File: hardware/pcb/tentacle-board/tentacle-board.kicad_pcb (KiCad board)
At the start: 2 copper layers, 55 x 55 mm, 74 parts, among them IC1 W25Q32JVZPIQ, J3 Conn_01x02, J5 Motor, J6 Motor, U1 NCP1117-3.3_SOT223, U3 RP2040, U4 DRV8825PWP, U5 DRV8825PWP, Y1 ABM8-12.000MHZ-20-B1U-T

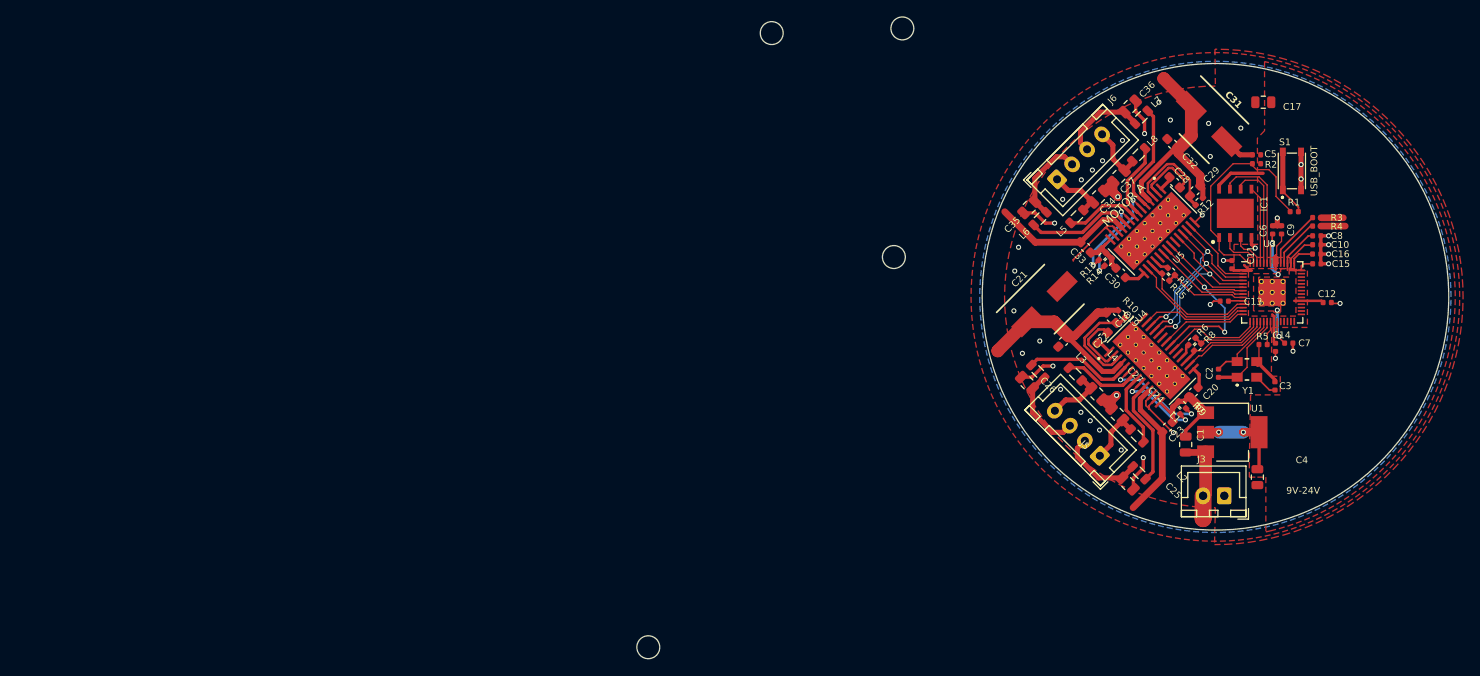
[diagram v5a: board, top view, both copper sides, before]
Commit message: Added aux plugs and updated the edge cuts
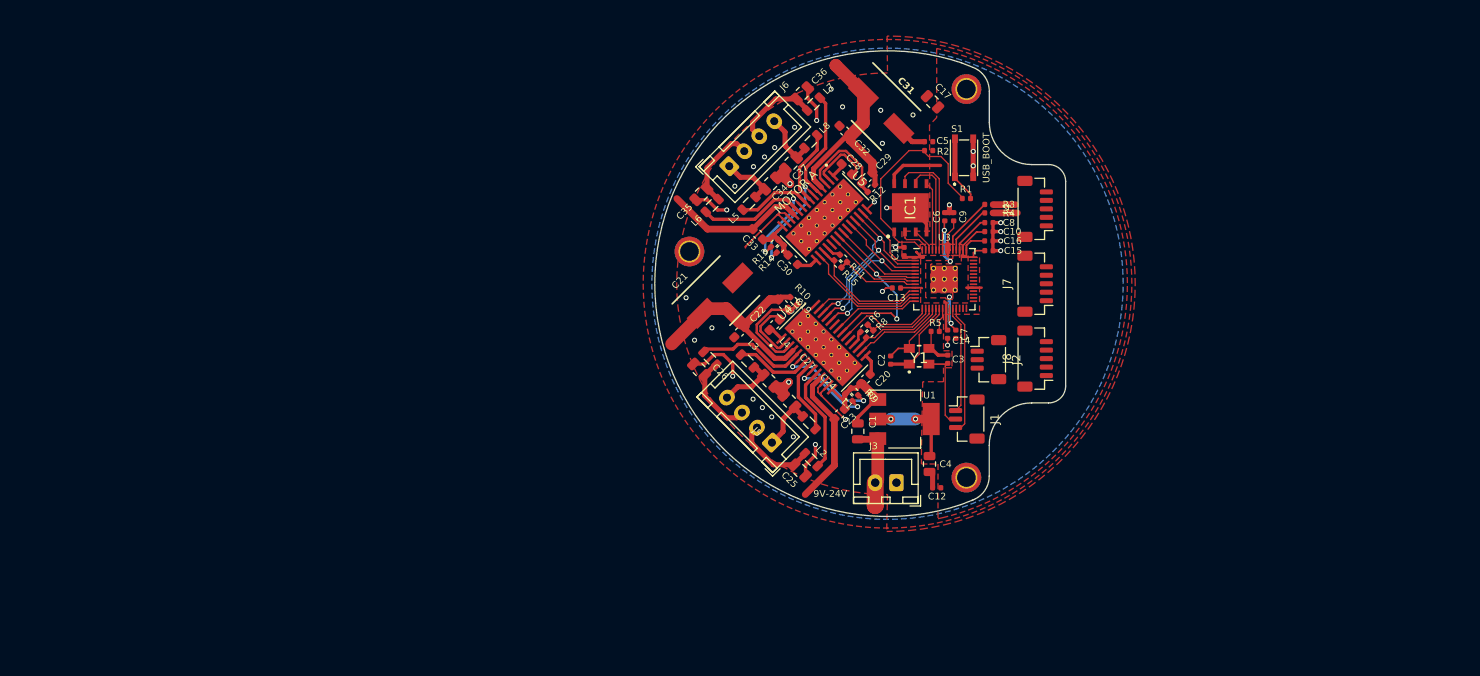
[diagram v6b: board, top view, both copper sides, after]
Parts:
- removed H2: MountingHole, MountingHole:MountingHole_2.7mm_M2.5
- added J1: DEBUG, Connector_JST:JST_SH_BM03B-SRSS-TB_1x03-1MP_P1.00mm_Vertical, F.Cu at (128.1, 109.7)
- added J2: UART0, Connector_JST:JST_SH_BM03B-SRSS-TB_1x03-1MP_P1.00mm_Vertical, F.Cu at (130.6, 102.7)
- added J4: Conn_01x05, Connector_JST:JST_SH_BM05B-SRSS-TB_1x05-1MP_P1.00mm_Vertical, F.Cu at (136.1, 84.9)
- added J7: Conn_01x05, Connector_JST:JST_SH_BM05B-SRSS-TB_1x05-1MP_P1.00mm_Vertical, F.Cu at (136.1, 93.7)
- added J8: Conn_01x05, Connector_JST:JST_SH_BM05B-SRSS-TB_1x05-1MP_P1.00mm_Vertical, F.Cu at (136.1, 102.5)
- H1, H3, H4: footprint MountingHole:MountingHole_2.7mm_M2.5 -> MountingHole:MountingHole_2.2mm_M2_ISO7380_Pad_TopBottom
- moved H4 75.7 mm to (128.0, 70.8)
- moved C12 51.0 mm to (124.5, 117.8), turned to 180 degrees
- moved C7 39.3 mm to (126.8, 99.7), turned to -90 degrees
- moved C17 39.0 mm to (124.0, 72.2), turned to 135 degrees
- moved C3 38.7 mm to (125.8, 102.6)
- moved L1 38.7 mm to (109.5, 110.1)
- moved R14 38.7 mm to (106.1, 89.6)
- moved C10 38.7 mm to (130.7, 87.5)
- moved C11 38.7 mm to (120.7, 89.9)
- moved C14 38.7 mm to (125.8, 99.6)
- moved C15 38.7 mm to (130.7, 89.8)
- moved C18 38.7 mm to (105.4, 98.5)
- moved C19 38.7 mm to (106.5, 96.2)
- moved C26 38.7 mm to (96.5, 103.8)
- moved C27 38.7 mm to (104.8, 105.1)
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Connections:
- IC1 pad 9: unconnected-(IC1-EP-Pad9) -> GND
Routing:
- net /SWD: track 0.00 -> 15.3 mm
- net GND: track 86.5 -> 101.2 mm, vias 40 -> 35
- net /SWCLK: track 0.00 -> 12.7 mm
- net +3V3: track 54.4 -> 52.4 mm
- net /QSPI_SD2: track 4.17 -> 2.78 mm
- net /QSPI_SD3: track 15.0 -> 13.8 mm
- net /QSPI_SCLK: track 12.9 -> 11.6 mm
- net /QSPI_SD1: track 5.17 -> 3.99 mm
- net Net-(Y1-X2): track 5.47 -> 4.42 mm
- net /QSPI_SD0: track 9.16 -> 8.11 mm
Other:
- board size 55 x 55 mm -> 48.4 x 54.9 mm

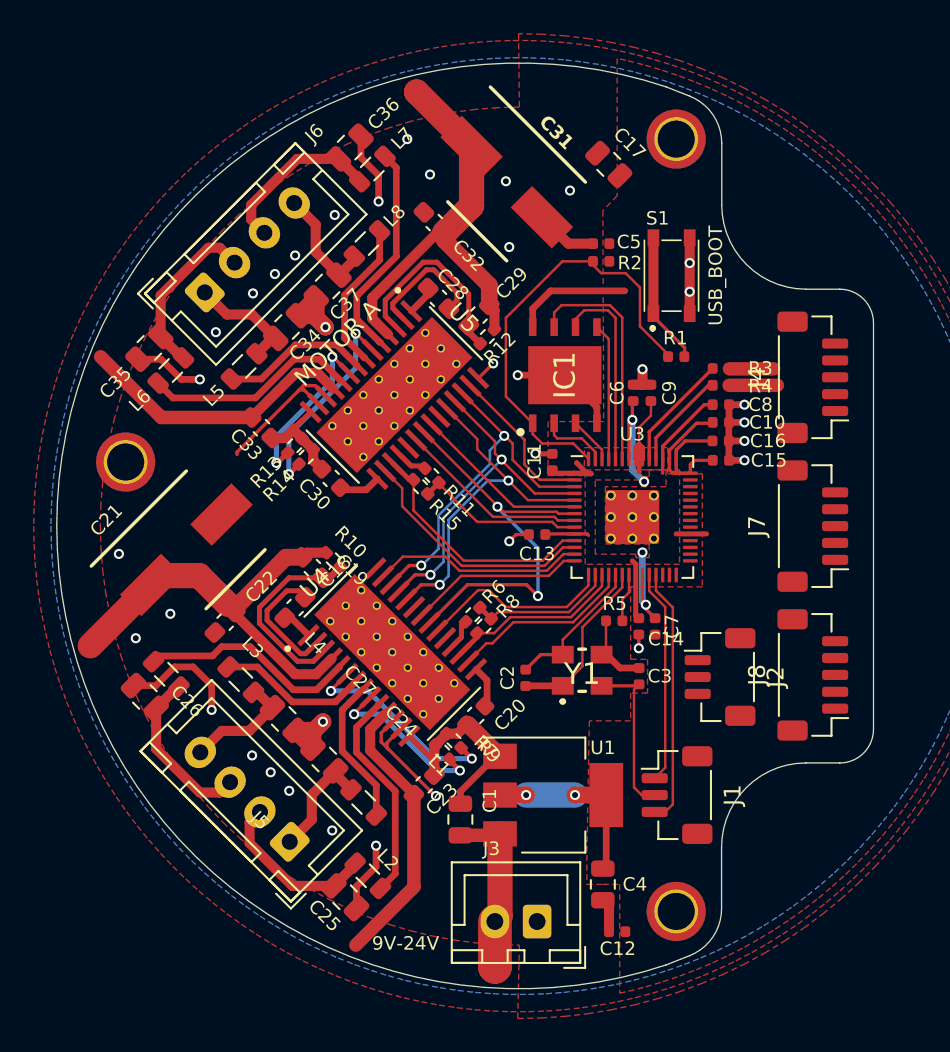
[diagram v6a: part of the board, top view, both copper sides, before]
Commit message: Finished component & trace layout
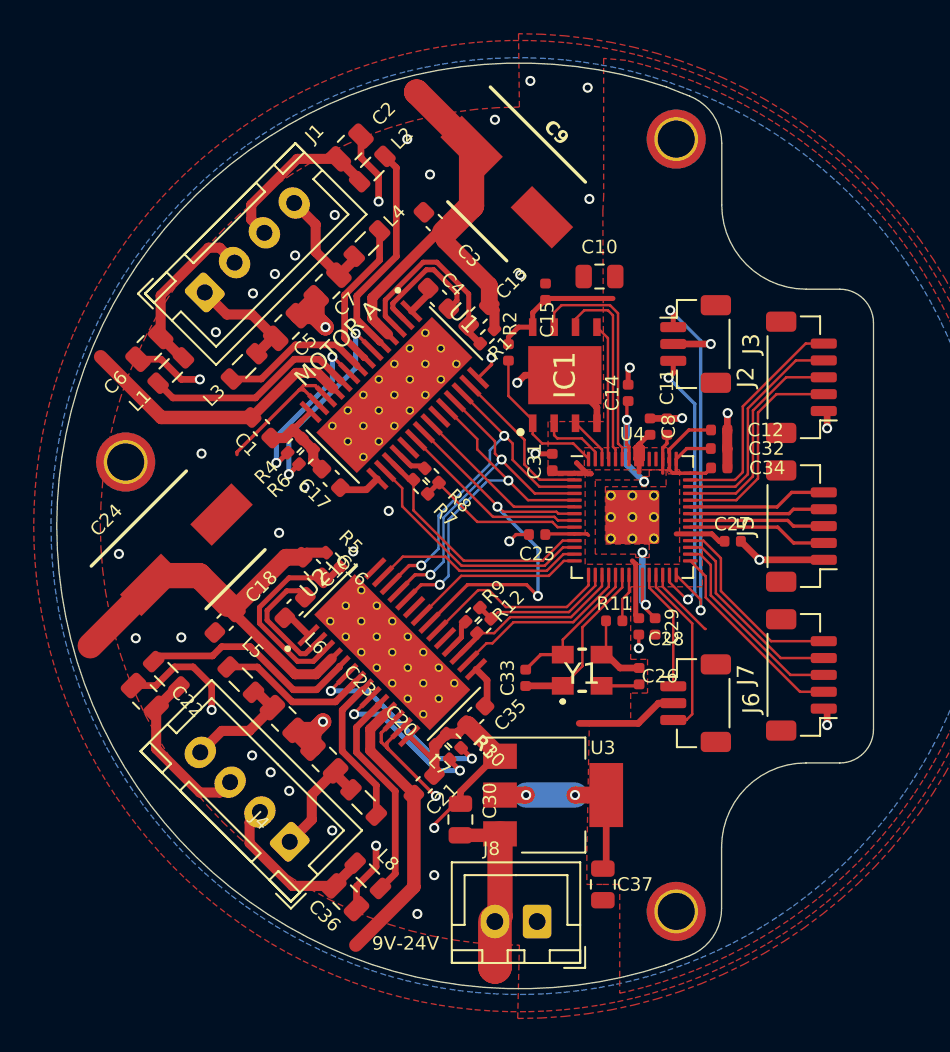
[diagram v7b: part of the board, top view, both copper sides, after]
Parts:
- removed the R1 at (128.0, 83.7)
- removed the R3 at (130.7, 84.3)
- removed the R4 at (130.7, 85.3)
- removed S1: PTS815_SJM_250_SMTR_LFS, tentacle-board:PTS815SJM250SMTRLFS
- added REF**: OSHW-Logo2_7.3x6mm_SilkScreen, Symbol:OSHW-Logo2_7.3x6mm_SilkScreen, F.Cu at (135.5, 93.7)
- moved C27 24.1 mm to (131.4, 94.6), turned to 0 degrees
- moved J3 19.8 mm to (129.2, 82.9)
- moved R2 7.71 mm to (118.1, 83.4), turned to -90 degrees
- moved C10 6.67 mm to (123.5, 78.9), turned to 180 degrees
- moved J6 5.56 mm to (129.2, 104.2)
- moved C15 4.36 mm to (120.3, 79.8), turned to 90 degrees
- moved C11 3.45 mm to (127.5, 87.8), turned to 90 degrees
- moved C8 2.00 mm to (126.5, 87.8)
- moved J2 0.67 mm to (135.5, 84.9)
- moved J5 0.67 mm to (135.5, 93.7)
- moved J7 0.67 mm to (135.5, 102.5)
- moved C12 0.46 mm to (130.6, 88.0)
- moved C34 0.46 mm to (130.6, 90.2)
- moved C32 0.46 mm to (130.6, 89.1)
- moved C14 0.30 mm to (125.2, 85.8)
- renumbered C33 to C1, C17 to C10, C8 to C11, C10 to C12, C29 to C13, C6 to C14, C5 to C15, C19 to C16, C30 to C17, C22 to C18, C18 to C19, C36 to C2, C24 to C20, C23 to C21, C26 to C22, C27 to C23, C21 to C24, C13 to C25, C3 to C26, C12 to C27, C14 to C28, C7 to C29, C32 to C3, C1 to C30, C11 to C31, C16 to C32, C2 to C33, C15 to C34, C20 to C35, C25 to C36, C4 to C37, C28 to C4, C34 to C5, C35 to C6, C37 to C7, C9 to C8, C31 to C9, H4 to H1, H1 to H2, J6 to J1, J4 to J2, J2 to J3, J5 to J4, J7 to J5, J1 to J6, J8 to J7, J3 to J8, L6 to L1, L7 to L2, L5 to L3, L8 to L4, L3 to L5, L4 to L6, L1 to L7, L2 to L8, R12 to R1, R9 to R10, R5 to R11, R8 to R12, R7 to R3, R13 to R4, R10 to R5, R14 to R6, R15 to R7, R11 to R8, R6 to R9, U5 to U1, U4 to U2, U1 to U3, U3 to U4
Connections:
- J2 pad 1: unconnected-(J4-Pin_1-Pad1) -> GND
- J2 pad 2: unconnected-(J4-Pin_2-Pad2) -> /GPIO26_ADC0
- J2 pad 3: unconnected-(J4-Pin_3-Pad3) -> /GPIO27_ADC1
- J2 pad 4: unconnected-(J4-Pin_4-Pad4) -> /GPIO28_ADC2
- J2 pad 5: unconnected-(J4-Pin_5-Pad5) -> /GPIO29_ADC3
- J5 pad 1: unconnected-(J7-Pin_1-Pad1) -> GND
- J5 pad 2: unconnected-(J7-Pin_2-Pad2) -> /GPIO22
- J5 pad 3: unconnected-(J7-Pin_3-Pad3) -> /GPIO23
- J5 pad 4: unconnected-(J7-Pin_4-Pad4) -> /GPIO24
- J5 pad 5: unconnected-(J7-Pin_5-Pad5) -> /GPIO25
- J7 pad 1: unconnected-(J8-Pin_1-Pad1) -> GND
- J7 pad 2: unconnected-(J8-Pin_2-Pad2) -> /GPIO18
- J7 pad 3: unconnected-(J8-Pin_3-Pad3) -> /GPIO19
- J7 pad 4: unconnected-(J8-Pin_4-Pad4) -> /GPIO20
- J7 pad 5: unconnected-(J8-Pin_5-Pad5) -> /GPIO21
- U4 pad 46: Net-(U3-USB_DM) -> unconnected-(U3-USB_DM-Pad46)
- U4 pad 47: Net-(U3-USB_DP) -> unconnected-(U3-USB_DP-Pad47)
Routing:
- net /GPIO17: track 0.00 -> 22.4 mm, vias 0 -> 2
- net /QSPI_SS: track 26.4 -> 8.89 mm
- net /GPIO16: track 0.00 -> 17.0 mm, vias 0 -> 2
- net /GPIO29_ADC3: track 0.00 -> 13.5 mm
- net /GPIO28_ADC2: track 0.00 -> 13.3 mm
- net /GPIO27_ADC1: track 0.00 -> 13.0 mm
- net /GPIO26_ADC0: track 0.00 -> 12.8 mm
- net /GPIO19: track 0.00 -> 11.9 mm
- net /GPIO18: track 0.00 -> 11.9 mm
- net /GPIO20: track 0.00 -> 11.7 mm
- net /GPIO21: track 0.00 -> 11.5 mm
- net /GPIO22: track 0.00 -> 8.30 mm
- net /GPIO25: track 0.00 -> 8.27 mm
- net /GPIO23: track 0.00 -> 8.05 mm
- net /GPIO24: track 0.00 -> 8.02 mm
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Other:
- board text removed: "USB_BOOT"

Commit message: Finished v1 and created manufacturing outputs
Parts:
- removed the REF** at (135.5, 93.7)
- added FID1: Fiducial, Fiducial:Fiducial_0.5mm_Mask1mm, F.Cu at (121.0, 67.8)
- added FID2: Fiducial, Fiducial:Fiducial_0.5mm_Mask1mm, F.Cu at (129.2, 113.8)
- added FID3: Fiducial, Fiducial:Fiducial_0.5mm_Mask1mm, F.Cu at (98.3, 89.0)
- added R13: 1.5k, Resistor_SMD:R_0402_1005Metric_Pad0.72x0.64mm_HandSolder, F.Cu at (130.3, 100.2)
- added REF**: OSHW-Symbol_6.7x6mm_SilkScreen, Symbol:OSHW-Symbol_6.7x6mm_SilkScreen, F.Cu at (131.0, 84.6)
- added VR1: TC33X-2-103E, tentacle-board:TC33X2503E, F.Cu at (125.4, 77.2)
- C10, C30, C37: value 10u -> 10uF
- C11, C12: value 1u -> 1uF
- C14, C15, C25, C27, C28, C29, C31, C32, C34, C8: value 100n -> 100nF
- C26, C33: value 27p -> 30pF
- J2: value Conn_01x05 -> AUX2
- J5: value Conn_01x05 -> AUX1
- J7: value Conn_01x05 -> CTRL
- R2: value DNF -> 10k; footprint Capacitor_SMD:C_0402_1005Metric -> Resistor_SMD:R_0402_1005Metric
- moved C10 9.30 mm to (123.6, 69.6)
- moved C12 0.90 mm to (129.7, 88.0)
- moved R2 0.20 mm to (118.1, 83.6)
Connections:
- net /Motor Driver/A1 renamed /Motor Driver B/A1
- net /Motor Driver/A2 renamed /Motor Driver B/A2
- net /Motor Driver/B1 renamed /Motor Driver B/B1
- net /Motor Driver/B2 renamed /Motor Driver B/B2
- net /Motor Driver1/A1 renamed /Motor Driver A/A1
- net /Motor Driver1/A2 renamed /Motor Driver A/A2
- net /Motor Driver1/B1 renamed /Motor Driver A/B1
- net /Motor Driver1/B2 renamed /Motor Driver A/B2
- J7 pad 2: /GPIO18 -> /RUN
- U1 pad 12: /Motor Driver1/VREF -> /Motor Driver A/VREF
- U1 pad 13: /Motor Driver1/VREF -> /Motor Driver A/VREF
- U2 pad 12: /Motor Driver/VREF -> /Motor Driver A/VREF
- U2 pad 13: /Motor Driver/VREF -> /Motor Driver A/VREF
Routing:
- net /Motor Driver A/VREF: track 0.00 -> 75.7 mm, vias 0 -> 3
- net GND: track 99.4 -> 119.6 mm, vias 45 -> 61
- net /GPIO18: track 11.9 -> 0.00 mm
- net /Motor Driver1/VREF: track 8.81 -> 0.00 mm
- net /RUN: track 4.28 -> 12.9 mm
- net /Motor Driver/VREF: track 7.85 -> 0.00 mm, vias 1 -> 0
- net VDC: track 95.5 -> 93.5 mm
- net /GPIO17: track 22.4 -> 23.3 mm
- net +3V3: track 51.3 -> 50.4 mm
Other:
- board text added: "9-20V"
- board text added: "Squeaky Robot"
- board text added: "Tentacle Controller"
- board text added: "V1.0"
